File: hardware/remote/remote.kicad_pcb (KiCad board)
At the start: 2 copper layers, 46.5 x 66 mm, 17 parts, among them SW1 UP, SW2 DOWN, SW3 ON/OFF, U1 TP4056-Module, U2 ME6211C33M5G, U3 ESP32-DevKitC-30

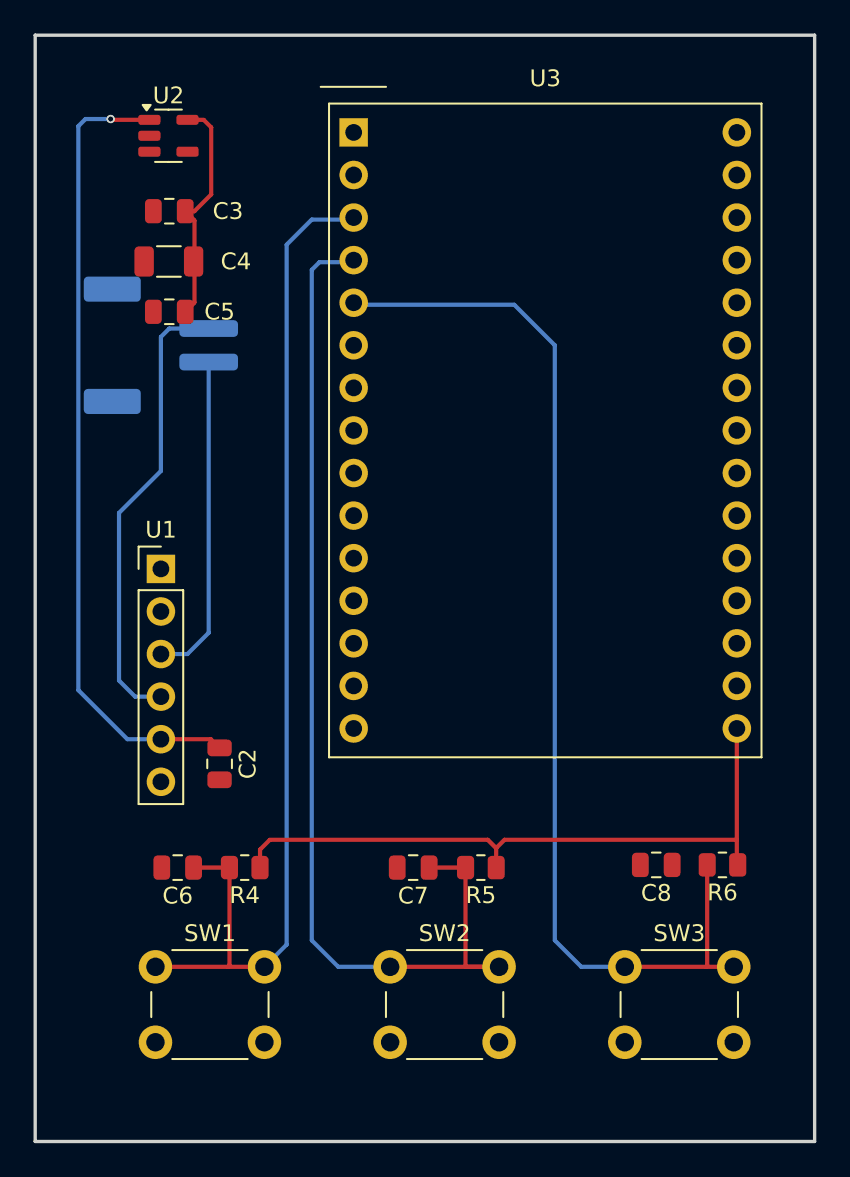
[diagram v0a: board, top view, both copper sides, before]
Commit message: hardware(remote): PCB layout tweaks, README rewrite, ignore ERC/DRC reports
Co-Authored-By: Claude Sonnet 5 <noreply@anthropic.com>
Claude-Session: https://claude.ai/code/session_01EpJvfsWNhnzVoGz5gYoJZP
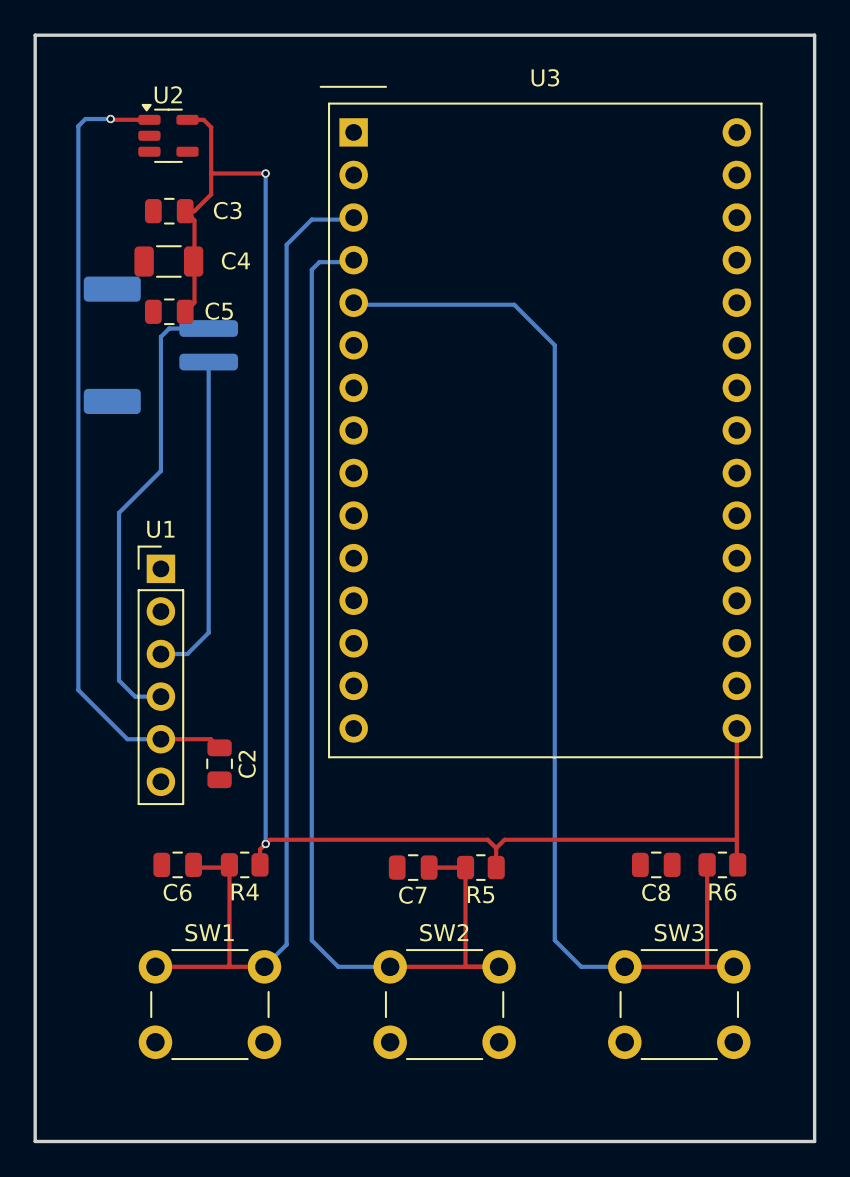
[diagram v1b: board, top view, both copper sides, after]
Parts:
- moved C6 0.16 mm to (124.5, 99.5)
- moved R4 0.16 mm to (128.5, 99.5)
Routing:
- net +3V3: track 53.4 -> 96.7 mm, vias 0 -> 2
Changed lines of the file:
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@@
 	(footprint "R_0805_2012Metric"
 		(layer "F.Cu")
-		(at 128.5 99.66 180)
+		(at 128.5 99.5 180)
 		(descr "Resistor SMD 0805 (2012 Metric), square (rectangular) end terminal, IPC_7351 nominal, (Body size source: IPC-SM-782 page 72, https://www.pcb-3d.com/wordpress/wp-content/uploads/ipc-sm-782a_amendment_1_and_2.pdf), generated with kicad-footprint-generator")
 		(tags "resistor")
@@
 	(footprint "C_0805_2012Metric"
 		(layer "F.Cu")
-		(at 124.5 99.66 180)
+		(at 124.5 99.5 180)
 		(descr "Capacitor SMD 0805 (2012 Metric), square (rectangular) end terminal, IPC_7351 nominal, (Body size source: IPC-SM-782 page 76, https://www.pcb-3d.com/wordpress/wp-content/uploads/ipc-sm-782a_amendment_1_and_2.pdf, https://docs.google.com/spreadsheets/d/1BsfQQcO9C6DZCsRaXUlFlo91Tg2WpOkGARC1WS5S8t0/edit?usp=sharing), generated with kicad-footprint-generator")
 		(tags "capacitor")
@@
 	)
 	(segment
-		(start 126.5 59.5)
+		(start 126.5 58.25)
 		(end 126.5 55.5)
 		(width 0.25)
@@
 	)
 	(segment
+		(start 129.4125 98.5875)
+		(end 129.75 98.25)
+		(width 0.25)
+		(layer "F.Cu")
+		(net "+3V3")
+	)
+	(segment
 		(start 126.05 55.05)
 		(end 125.0875 55.05)
@@
 	)
 	(segment
+		(start 126.5 59.5)
+		(end 126.5 58.25)
+		(width 0.25)
+		(layer "F.Cu")
+		(net "+3V3")
+	)
+	(segment
 		(start 126.5 55.5)
 		(end 126.05 55.05)
@@
 	)
 	(segment
-		(start 129.4125 98.5875)
+		(start 129.75 98.25)
 		(end 130 98)
 		(width 0.25)
@@
 	)
 	(segment
+		(start 126.5 58.25)
+		(end 129.75 58.25)
+		(width 0.25)
+		(layer "F.Cu")
+		(net "+3V3")
+	)
+	(segment
 		(start 125.5 65.95)
 		(end 125.5 63.55)
@@
 		(net "+3V3")
 	)
+	(via
+		(at 129.75 98.25)
+		(size 0.5)
+		(drill 0.3)
+		(layers "F.Cu" "B.Cu")
+		(net "+3V3")
+	)
+	(via
+		(at 129.75 58.25)
+		(size 0.5)
+		(drill 0.3)
+		(layers "F.Cu" "B.Cu")
+		(net "+3V3")
+	)
 	(segment
-		(start 157.675 105.58)
-		(end 156 105.58)
+		(start 129.75 58.25)
+		(end 129.75 98.25)
+		(width 0.25)
+		(layer "B.Cu")
+		(net "+3V3")
+	)
+	(segment
+		(start 141.675 105.58)
+		(end 141.675 99.66)
 		(width 0.25)
 		(layer "F.Cu")
-		(net "/BTN_ONOFF")
+		(net "/BTN_DOWN")
 	)
 	(segment
-		(start 156.0875 99.5)
-		(end 156.0875 105.4925)
+		(start 139.5 99.66)
+		(end 141.675 99.66)
 		(width 0.25)
 		(layer "F.Cu")
-		(net "/BTN_ONOFF")
+		(net "/BTN_DOWN")
 	)
 	(segment
-		(start 156 105.58)
-		(end 151.175 105.58)
+		(start 137.175 105.58)
+		(end 143.675 105.58)
 		(width 0.25)
 		(layer "F.Cu")
-		(net "/BTN_ONOFF")
+		(net "/BTN_DOWN")
 	)
 	(segment
-		(start 156.0875 105.4925)
-		(end 156 105.58)
+		(start 143.675 105.58)
+		(end 141.675 105.58)
 		(width 0.25)
 		(layer "F.Cu")
-		(net "/BTN_ONOFF")
+		(net "/BTN_DOWN")
 	)
 	(segment
-		(start 147 68.5)
-		(end 147 104)
+		(start 134.08 105.58)
+		(end 137.175 105.58)
 		(width 0.25)
 		(layer "B.Cu")
-		(net "/BTN_ONOFF")
+		(net "/BTN_DOWN")
 	)
 	(segment
-		(start 148.58 105.58)
-		(end 151.175 105.58)
+		(start 135 63.54)
+		(end 132.96 63.54)
 		(width 0.25)
 		(layer "B.Cu")
-		(net "/BTN_ONOFF")
+		(net "/BTN_DOWN")
 	)
 	(segment
-		(start 147 104)
-		(end 148.58 105.58)
+		(start 132.5 104)
+		(end 134.08 105.58)
 		(width 0.25)
 		(layer "B.Cu")
-		(net "/BTN_ONOFF")
+		(net "/BTN_DOWN")
 	)
 	(segment
-		(start 135 66.08)
-		(end 144.58 66.08)
+		(start 132.5 64)
+		(end 132.5 104)
 		(width 0.25)
 		(layer "B.Cu")
-		(net "/BTN_ONOFF")
+		(net "/BTN_DOWN")
 	)
 	(segment
-		(start 144.58 66.08)
-		(end 147 68.5)
+		(start 132.96 63.54)
+		(end 132.5 64)
 		(width 0.25)
 		(layer "B.Cu")
-		(net "/BTN_ONOFF")
+		(net "/BTN_DOWN")
 	)
 	(segment
-		(start 141.675 105.58)
-		(end 141.675 99.66)
+		(start 122.8125 55.05)
+		(end 120.55 55.05)
 		(width 0.25)
 		(layer "F.Cu")
-		(net "/BTN_DOWN")
+		(net "/VSYS")
 	)
 	(segment
-		(start 139.5 99.66)
-		(end 141.675 99.66)
+		(start 123.5 92)
+		(end 126.48 92)
 		(width 0.25)
 		(layer "F.Cu")
-		(net "/BTN_DOWN")
+		(net "/VSYS")
 	)
 	(segment
-		(start 137.175 105.58)
-		(end 143.675 105.58)
+		(start 126.48 92)
+		(end 127 92.52)
 		(width 0.25)
 		(layer "F.Cu")
-		(net "/BTN_DOWN")
+		(net "/VSYS")
 	)
 	(segment
-		(start 143.675 105.58)
-		(end 141.675 105.58)
+		(start 120.55 55.05)
+		(end 120.5 55)
 		(width 0.25)
 		(layer "F.Cu")
-		(net "/BTN_DOWN")
+		(net "/VSYS")
+	)
+	(via
+		(at 120.5 55)
+		(size 0.5)
+		(drill 0.3)
+		(layers "F.Cu" "B.Cu")
+		(net "/VSYS")
 	)
 	(segment
-		(start 134.08 105.58)
-		(end 137.175 105.58)
+		(start 118.575 55.425)
+		(end 118.575 89.075)
 		(width 0.25)
 		(layer "B.Cu")
-		(net "/BTN_DOWN")
+		(net "/VSYS")
 	)
 	(segment
-		(start 135 63.54)
-		(end 132.96 63.54)
+		(start 121.5 92)
+		(end 123.5 92)
 		(width 0.25)
 		(layer "B.Cu")
-		(net "/BTN_DOWN")
+		(net "/VSYS")
 	)
 	(segment
-		(start 132.5 104)
-		(end 134.08 105.58)
+		(start 120.5 55)
+		(end 119 55)
 		(width 0.25)
 		(layer "B.Cu")
-		(net "/BTN_DOWN")
+		(net "/VSYS")
 	)
 	(segment
-		(start 132.5 64)
-		(end 132.5 104)
+		(start 119 55)
+		(end 118.575 55.425)
 		(width 0.25)
 		(layer "B.Cu")
-		(net "/BTN_DOWN")
+		(net "/VSYS")
 	)
 	(segment
-		(start 132.96 63.54)
-		(end 132.5 64)
+		(start 118.575 89.075)
+		(end 121.5 92)
 		(width 0.25)
 		(layer "B.Cu")
-		(net "/BTN_DOWN")
+		(net "/VSYS")
+	)
+	(segment
+		(start 157.675 105.58)
+		(end 156 105.58)
+		(width 0.25)
+		(layer "F.Cu")
+		(net "/BTN_ONOFF")
+	)
+	(segment
+		(start 156.0875 99.5)
+		(end 156.0875 105.4925)
+		(width 0.25)
+		(layer "F.Cu")
+		(net "/BTN_ONOFF")
+	)
+	(segment
+		(start 156 105.58)
+		(end 151.175 105.58)
+		(width 0.25)
+		(layer "F.Cu")
+		(net "/BTN_ONOFF")
+	)
+	(segment
+		(start 156.0875 105.4925)
+		(end 156 105.58)
+		(width 0.25)
+		(layer "F.Cu")
+		(net "/BTN_ONOFF")
+	)
+	(segment
+		(start 147 68.5)
+		(end 147 104)
+		(width 0.25)
+		(layer "B.Cu")
+		(net "/BTN_ONOFF")
+	)
+	(segment
+		(start 148.58 105.58)
+		(end 151.175 105.58)
+		(width 0.25)
+		(layer "B.Cu")
+		(net "/BTN_ONOFF")
+	)
+	(segment
+		(start 147 104)
+		(end 148.58 105.58)
+		(width 0.25)
+		(layer "B.Cu")
+		(net "/BTN_ONOFF")
+	)
+	(segment
+		(start 135 66.08)
+		(end 144.58 66.08)
+		(width 0.25)
+		(layer "B.Cu")
+		(net "/BTN_ONOFF")
+	)
+	(segment
+		(start 144.58 66.08)
+		(end 147 68.5)
+		(width 0.25)
+		(layer "B.Cu")
+		(net "/BTN_ONOFF")
 	)
 	(segment
@@
 		(net "/BATT_N")
 	)
-	(segment
-		(start 122.8125 55.05)
-		(end 120.55 55.05)
-		(width 0.25)
-		(layer "F.Cu")
-		(net "/VSYS")
-	)
-	(segment
-		(start 123.5 92)
-		(end 126.48 92)
-		(width 0.25)
-		(layer "F.Cu")
-		(net "/VSYS")
-	)
-	(segment
-		(start 126.48 92)
-		(end 127 92.52)
-		(width 0.25)
-		(layer "F.Cu")
-		(net "/VSYS")
-	)
-	(segment
-		(start 120.55 55.05)
-		(end 120.5 55)
-		(width 0.25)
-		(layer "F.Cu")
-		(net "/VSYS")
-	)
-	(via
-		(at 120.5 55)
-		(size 0.5)
-		(drill 0.3)
-		(layers "F.Cu" "B.Cu")
-		(net "/VSYS")
-	)
-	(segment
-		(start 118.575 55.425)
-		(end 118.575 89.075)
-		(width 0.25)
-		(layer "B.Cu")
-		(net "/VSYS")
-	)
-	(segment
-		(start 121.5 92)
-		(end 123.5 92)
-		(width 0.25)
-		(layer "B.Cu")
-		(net "/VSYS")
-	)
-	(segment
-		(start 120.5 55)
-		(end 119 55)
-		(width 0.25)
-		(layer "B.Cu")
-		(net "/VSYS")
-	)
-	(segment
-		(start 119 55)
-		(end 118.575 55.425)
-		(width 0.25)
-		(layer "B.Cu")
-		(net "/VSYS")
-	)
-	(segment
-		(start 118.575 89.075)
-		(end 121.5 92)
-		(width 0.25)
-		(layer "B.Cu")
-		(net "/VSYS")
-	)
 	(zone
